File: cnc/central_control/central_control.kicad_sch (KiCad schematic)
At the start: 112 parts, among them J1 DE9_Receptacle, J2 AVR-UPDI, J3 7pins, J4 Phoenix, J5 6pins, J6 6pins, J7 6pins, J8 3pins, J9 4pins, Q1 BSS138, U1 ATtiny1626-S, U10 PC817, U2 PC817, U3 PC817, U4 PCA9555PW, U5 LT1785AxS8, U7 LMR33630ADDA, U8 PC817, U9 PCA9555PW

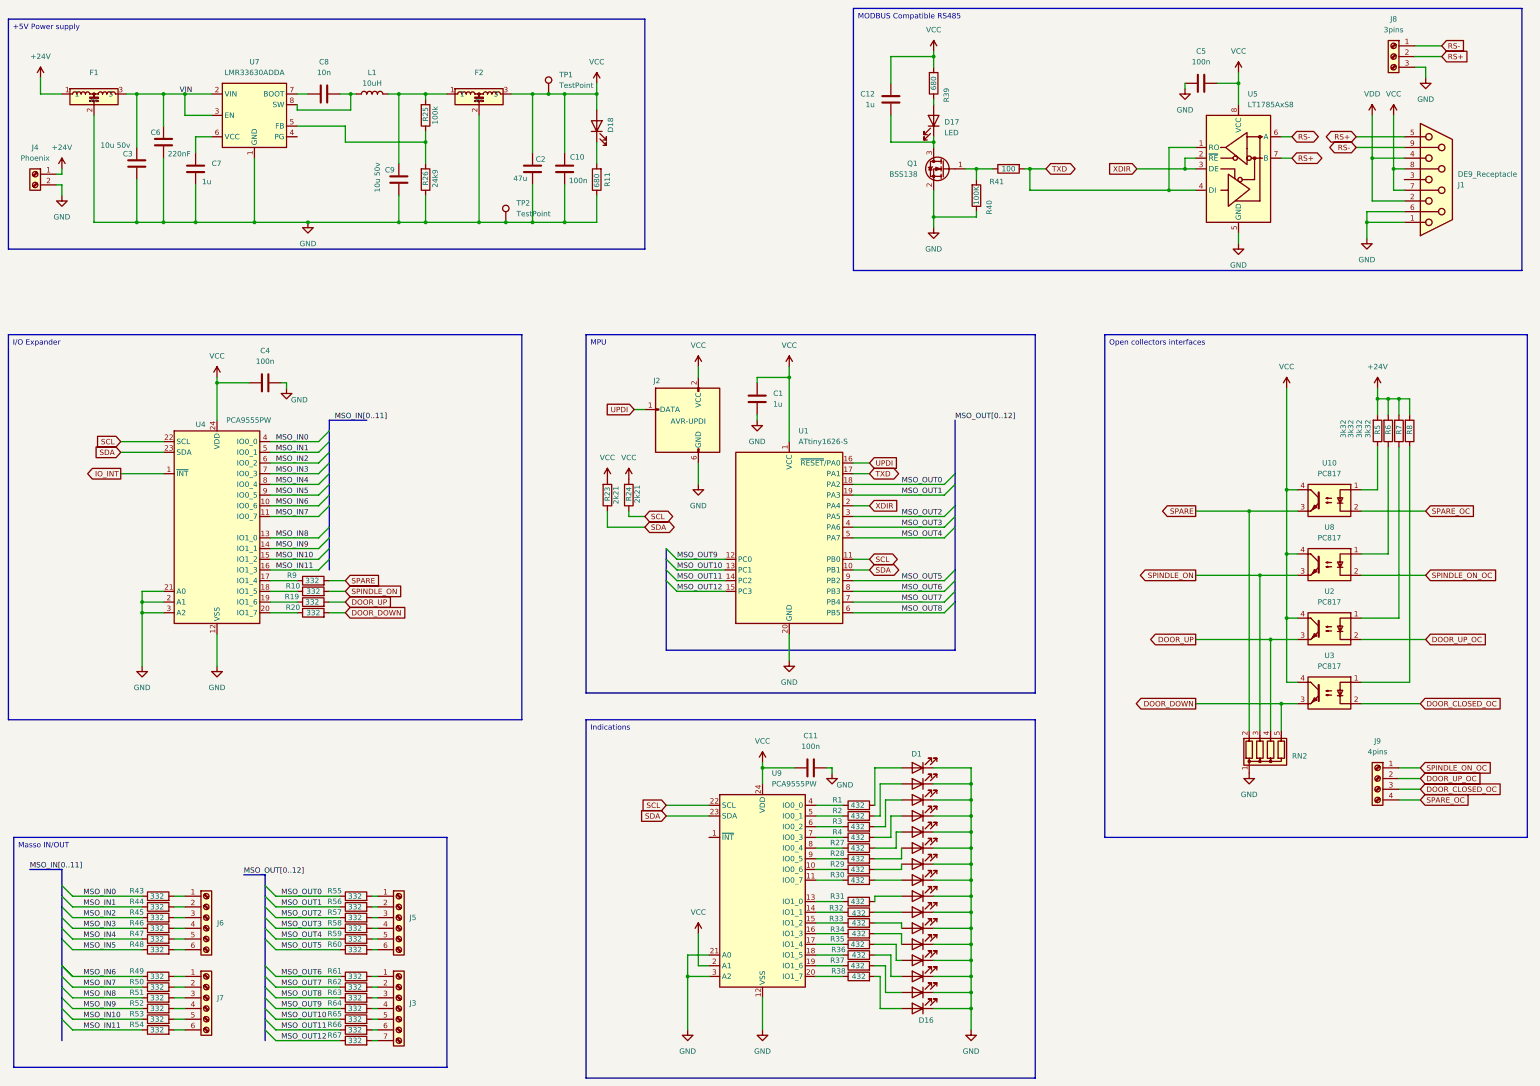
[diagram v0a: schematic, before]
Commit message: Split sheets
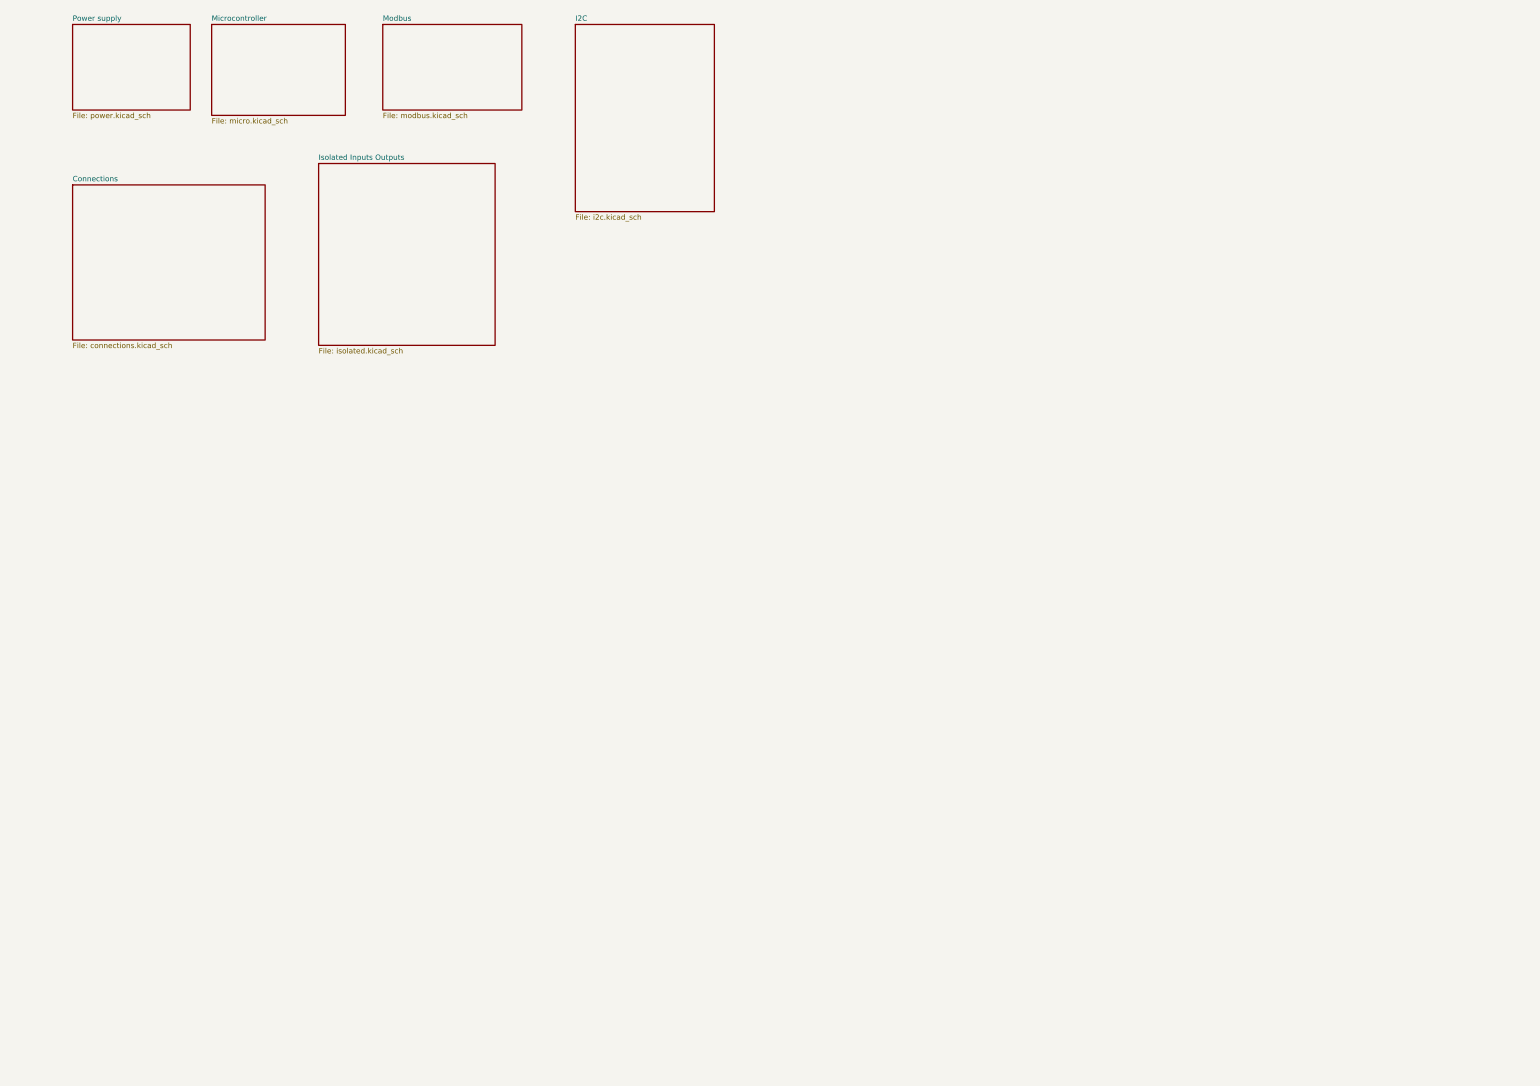
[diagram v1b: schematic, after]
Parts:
- removed C1, C7: 1u, Capacitor_SMD:C_0805_2012Metric_Pad1.18x1.45mm_HandSolder, symbol Device:C
- removed C10, C11, C4, C5: 100n, Capacitor_SMD:C_0603_1608Metric_Pad1.08x0.95mm_HandSolder, symbol Device:C
- removed C12: 1u, Capacitor_SMD:C_0603_1608Metric_Pad1.08x0.95mm_HandSolder, symbol Device:C
- removed C2: 47u, Capacitor_SMD:C_1210_3225Metric_Pad1.33x2.70mm_HandSolder, symbol Device:C
- removed C3, C9: 10u 50v, Capacitor_SMD:C_1210_3225Metric_Pad1.33x2.70mm_HandSolder, symbol Device:C
- removed C6: 220nF, Capacitor_SMD:C_0805_2012Metric_Pad1.18x1.45mm_HandSolder, symbol Device:C
- removed C8: 10n, Capacitor_SMD:C_0805_2012Metric_Pad1.18x1.45mm_HandSolder, symbol Device:C
- removed D1, D10, D11, D12, D13, D14, D15, D16, D17, D18, D2, D3, D4, D5, D6, D7, D8, D9: LED, LED_THT:LED_D3.0mm, symbol Device:LED
- removed F1, F2: ~, Adarwoo:Murata_NFM61R, symbol ARex:NFM611R30
- removed J1: DE9_Receptacle, Connector_Dsub:DSUB-9_Female_Vertical_P2.77x2.84mm_MountingHoles, symbol Connector:DE9_Receptacle
- removed J2: AVR-UPDI, Connector_PinHeader_2.54mm:PinHeader_2x03_P2.54mm_Vertical, symbol Connector:AVR-UPDI-6
- removed J3: 7pins, Connector_Phoenix_MC:PhoenixContact_MCV_1,5_7-G-3.81_1x07_P3.81mm_Vertical, symbol Connector:Screw_Terminal_01x07
- removed J4: Phoenix, Connector_Phoenix_MC:PhoenixContact_MCV_1,5_2-G-3.81_1x02_P3.81mm_Vertical, symbol Connector:Screw_Terminal_01x02
- removed J5, J6, J7: 6pins, Connector_Phoenix_MC:PhoenixContact_MCV_1,5_6-G-3.81_1x06_P3.81mm_Vertical, symbol Connector:Screw_Terminal_01x06
- removed J8: 3pins, Connector_Phoenix_MC:PhoenixContact_MCV_1,5_3-G-3.81_1x03_P3.81mm_Vertical, symbol Connector:Screw_Terminal_01x03
- removed J9: 4pins, Connector_Phoenix_MC:PhoenixContact_MCV_1,5_4-G-3.81_1x04_P3.81mm_Vertical, symbol Connector:Screw_Terminal_01x04
- removed L1: 10uH, Inductor_SMD:L_Wuerth_HCM-7070, symbol Device:L
- removed Q1: BSS138, Package_TO_SOT_SMD:SOT-23, symbol Transistor_FET:BSS138
- removed R1, R2, R27, R28, R29, R3, R30, R31, R32, R33, R34, R35, R36, R37, R38, R4: 432, Resistor_SMD:R_1206_3216Metric_Pad1.30x1.75mm_HandSolder, symbol Device:R
- removed R10, R19, R20, R43, R44, R45, R46, R47, R48, R49, R50, R51, R52, R53, R54, R55, R56, R57, R58, R59, R60, R61, R62, R63, R64, R65, R66, R67, R9: 332, Resistor_SMD:R_0805_2012Metric_Pad1.20x1.40mm_HandSolder, symbol Device:R
- removed R11, R39: 680, Resistor_SMD:R_1206_3216Metric_Pad1.30x1.75mm_HandSolder, symbol Device:R
- removed R23, R24: 2k21, Resistor_SMD:R_1206_3216Metric_Pad1.30x1.75mm_HandSolder, symbol Device:R
- removed R25: 100k, Resistor_SMD:R_0603_1608Metric_Pad0.98x0.95mm_HandSolder, symbol Device:R
- removed R26: 24k9, Resistor_SMD:R_0603_1608Metric_Pad0.98x0.95mm_HandSolder, symbol Device:R
- removed R40: 100K, Resistor_SMD:R_1206_3216Metric_Pad1.30x1.75mm_HandSolder, symbol Device:R
- removed R41: 100, Resistor_SMD:R_1206_3216Metric_Pad1.30x1.75mm_HandSolder, symbol Device:R
- removed R5, R6, R7, R8: 3k32, Resistor_SMD:R_1206_3216Metric_Pad1.30x1.75mm_HandSolder, symbol Device:R
- removed RN2: R_Network04, Resistor_THT:R_Array_SIP5, symbol Device:R_Network04
- removed TP1, TP2: TestPoint, TestPoint:TestPoint_Loop_D3.50mm_Drill0.9mm_Beaded, symbol Connector:TestPoint
- removed U1: ATtiny1626-S, Package_SO:SOIC-20W_7.5x12.8mm_P1.27mm, symbol MCU_Microchip_ATtiny:ATtiny3226-S
- removed U10, U2, U3, U8: PC817, Package_DIP:DIP-4_W10.16mm, symbol Isolator:PC817
- removed U4, U9: PCA9555PW, Package_SO:TSSOP-24_4.4x7.8mm_P0.65mm, symbol Interface_Expansion:PCA9555PW
- removed U5: LT1785AxS8, Package_SO:SOIC-8_3.9x4.9mm_P1.27mm, symbol Interface_UART:LT1785AxS8
- removed U7: LMR33630ADDA, Package_SO:Texas_HSOP-8-1EP_3.9x4.9mm_P1.27mm_ThermalVias, symbol Regulator_Switching:LMR33630ADDA
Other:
- added sheet Connections (connections.kicad_sch)
- added sheet I2C (i2c.kicad_sch)
- added sheet Isolated Inputs Outputs (isolated.kicad_sch)
- added sheet Microcontroller (micro.kicad_sch)
- added sheet Modbus (modbus.kicad_sch)
- added sheet Power supply (power.kicad_sch)

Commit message: On-going
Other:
- removed sheet Modbus
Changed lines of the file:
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@@
 (kicad_sch
-	(version 20231120)
+	(version 20250114)
 	(generator "eeschema")
-	(generator_version "8.0")
+	(generator_version "9.0")
 	(paper "A4")
 	(title_block
@@
 		(at 156.21 27.94)
 		(size 33.02 44.45)
+		(exclude_from_sim no)
+		(in_bom yes)
+		(on_board yes)
+		(dnp no)
 		(fields_autoplaced yes)
 		(stroke
@@
 		(at 69.85 27.94)
 		(size 31.75 21.59)
+		(exclude_from_sim no)
+		(in_bom yes)
+		(on_board yes)
+		(dnp no)
 		(fields_autoplaced yes)
 		(stroke
@@
 		(at 36.83 27.94)
 		(size 27.94 20.32)
+		(exclude_from_sim no)
+		(in_bom yes)
+		(on_board yes)
+		(dnp no)
 		(fields_autoplaced yes)
 		(stroke
@@
 		(at 36.83 66.04)
 		(size 45.72 36.83)
+		(exclude_from_sim no)
+		(in_bom yes)
+		(on_board yes)
+		(dnp no)
 		(fields_autoplaced yes)
 		(stroke
@@
 		(at 95.25 60.96)
 		(size 41.91 43.18)
+		(exclude_from_sim no)
+		(in_bom yes)
+		(on_board yes)
+		(dnp no)
 		(fields_autoplaced yes)
 		(stroke
@@
 				(path "/24bc57b9-acf8-493e-9df6-7015f7e1bb8a"
 					(page "5")
-				)
-			)
-		)
-	)
-	(sheet
-		(at 110.49 27.94)
-		(size 33.02 20.32)
-		(fields_autoplaced yes)
-		(stroke
-			(width 0.1524)
-			(type solid)
-		)
-		(fill
-			(color 0 0 0 0.0000)
-		)
-		(property "Sheetname" "Modbus"
-			(at 110.49 27.2284 0)
-			(effects
-				(font
-					(size 1.27 1.27)
-				)
-				(justify left bottom)
-			)
-		)
-		(property "Sheetfile" "modbus.kicad_sch"
-			(at 110.49 48.8446 0)
-			(effects
-				(font
-					(size 1.27 1.27)
-				)
-				(justify left top)
-			)
-		)
-		(instances
-			(project "central_control"
-				(path "/24bc57b9-acf8-493e-9df6-7015f7e1bb8a"
-					(page "4")
 				)
 			)
@@
 		)
 	)
+	(embedded_fonts no)
 )
